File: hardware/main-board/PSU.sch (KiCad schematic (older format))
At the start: 5 parts, among them U3 AP1509-33SG-13

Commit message: added all 3d
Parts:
- L1: footprint Inductor_SMD:L_Taiyo-Yuden_NR-60xx -> main-board-custom-footprints:L_Taiyo-Yuden_NR-60xx
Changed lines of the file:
@@
 F 0 "L1" V 7040 5000 50  0000 C CNN
 F 1 "47uH" V 6949 5000 50  0000 C CNN
-F 2 "Inductor_SMD:L_Taiyo-Yuden_NR-60xx" H 6850 5000 50  0001 C CNN
+F 2 "main-board-custom-footprints:L_Taiyo-Yuden_NR-60xx" H 6850 5000 50  0001 C CNN
 F 3 "~" H 6850 5000 50  0001 C CNN
 F 4 "NRS6045T470MMGKV" V 6850 5000 50  0001 C CNN "MPN"

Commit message: SO-8 3d added, layout done
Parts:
- U3: footprint Package_SO:SO-8_3.9x4.9mm_P1.27mm -> main-board-custom-footprints:SO-8_3.9x4.9mm_P1.27mm
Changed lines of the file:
@@
 F 0 "U3" H 5800 5565 50  0000 C CNN
 F 1 "AP1509-33SG-13" H 5800 5474 50  0000 C CNN
-F 2 "Package_SO:SO-8_3.9x4.9mm_P1.27mm" H 5750 5250 50  0001 C CNN
+F 2 "main-board-custom-footprints:SO-8_3.9x4.9mm_P1.27mm" H 5750 5250 50  0001 C CNN
 F 3 "" H 5750 5250 50  0001 C CNN
 F 4 "AP1509-33SG-13" H 5800 5150 50  0001 C CNN "MPN"

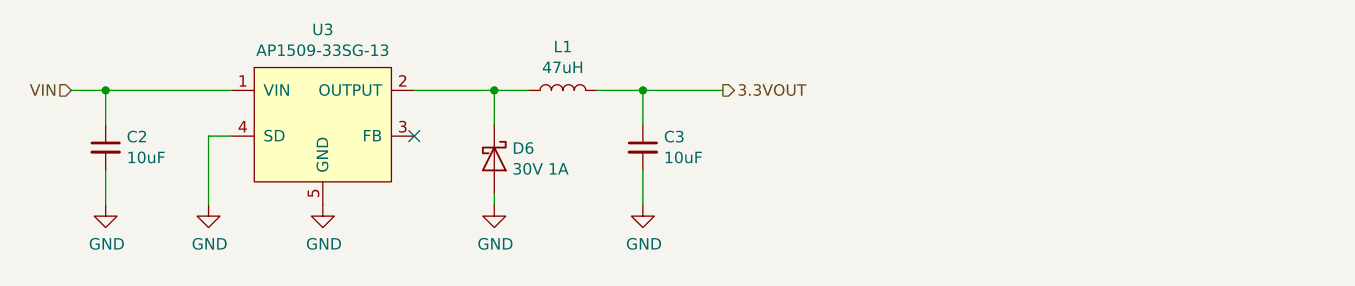
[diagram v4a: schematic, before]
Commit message: added qr code, switched button to a different button. put on reddit for review
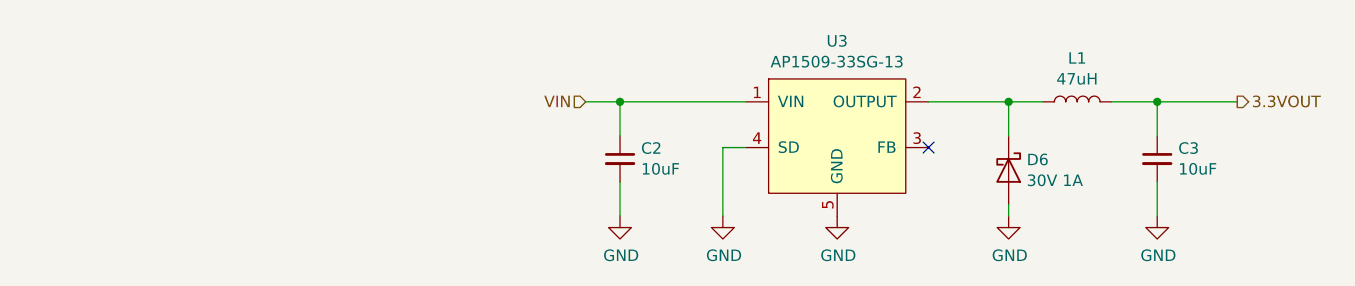
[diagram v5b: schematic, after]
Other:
- moved on the sheet: C2, C3, D6, L1, U3
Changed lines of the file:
@@
 EESchema Schematic File Version 4
-LIBS:main-board-cache
-EELAYER 29 0
+EELAYER 30 0
 EELAYER END
 $Descr B 17000 11000
@@
 L main-board-custom-symbols:AP1509-50 U3
 U 1 1 60FCBB15
-P 5800 5150
-F 0 "U3" H 5800 5565 50  0000 C CNN
-F 1 "AP1509-33SG-13" H 5800 5474 50  0000 C CNN
-F 2 "main-board-custom-footprints:SO-8_3.9x4.9mm_P1.27mm" H 5750 5250 50  0001 C CNN
-F 3 "" H 5750 5250 50  0001 C CNN
-F 4 "AP1509-33SG-13" H 5800 5150 50  0001 C CNN "MPN"
-	1    5800 5150
+P 8050 5200
+F 0 "U3" H 8050 5615 50  0000 C CNN
+F 1 "AP1509-33SG-13" H 8050 5524 50  0000 C CNN
+F 2 "main-board-custom-footprints:SO-8_3.9x4.9mm_P1.27mm" H 8000 5300 50  0001 C CNN
+F 3 "" H 8000 5300 50  0001 C CNN
+F 4 "AP1509-33SG-13" H 8050 5200 50  0001 C CNN "MPN"
+	1    8050 5200
 	1    0    0    -1
 $EndComp
-NoConn ~ 6200 5200
+NoConn ~ 8450 5250
 Wire Wire Line
-	5400 5200 5300 5200
+	7650 5250 7550 5250
 $Comp
 L power:GND #PWR019
 U 1 1 60FCC50A
-P 5800 5500
-F 0 "#PWR019" H 5800 5250 50  0001 C CNN
-F 1 "GND" H 5805 5327 50  0000 C CNN
-F 2 "" H 5800 5500 50  0001 C CNN
-F 3 "" H 5800 5500 50  0001 C CNN
-	1    5800 5500
+P 8050 5550
+F 0 "#PWR019" H 8050 5300 50  0001 C CNN
+F 1 "GND" H 8055 5377 50  0000 C CNN
+F 2 "" H 8050 5550 50  0001 C CNN
+F 3 "" H 8050 5550 50  0001 C CNN
+	1    8050 5550
 	1    0    0    -1
 $EndComp
@@
 L power:GND #PWR018
 U 1 1 60FCC70B
-P 5300 5500
-F 0 "#PWR018" H 5300 5250 50  0001 C CNN
-F 1 "GND" H 5305 5327 50  0000 C CNN
-F 2 "" H 5300 5500 50  0001 C CNN
-F 3 "" H 5300 5500 50  0001 C CNN
-	1    5300 5500
+P 7550 5550
+F 0 "#PWR018" H 7550 5300 50  0001 C CNN
+F 1 "GND" H 7555 5377 50  0000 C CNN
+F 2 "" H 7550 5550 50  0001 C CNN
+F 3 "" H 7550 5550 50  0001 C CNN
+	1    7550 5550
 	1    0    0    -1
 $EndComp
 Wire Wire Line
-	5300 5200 5300 5500
+	7550 5250 7550 5550
 $Comp
 L Device:C_Small C2
 U 1 1 60FCCE2C
-P 4850 5250
-F 0 "C2" H 4942 5296 50  0000 L CNN
-F 1 "10uF" H 4942 5205 50  0000 L CNN
-F 2 "Capacitor_SMD:C_1210_3225Metric" H 4850 5250 50  0001 C CNN
-F 3 "~" H 4850 5250 50  0001 C CNN
-	1    4850 5250
+P 7100 5300
+F 0 "C2" H 7192 5346 50  0000 L CNN
+F 1 "10uF" H 7192 5255 50  0000 L CNN
+F 2 "Capacitor_SMD:C_1210_3225Metric" H 7100 5300 50  0001 C CNN
+F 3 "~" H 7100 5300 50  0001 C CNN
+	1    7100 5300
 	1    0    0    -1
 $EndComp
 Wire Wire Line
-	5400 5000 4850 5000
+	7650 5050 7100 5050
 Wire Wire Line
-	4850 5000 4850 5150
+	7100 5050 7100 5200
 $Comp
 L power:GND #PWR017
 U 1 1 60FCD6A2
-P 4850 5500
-F 0 "#PWR017" H 4850 5250 50  0001 C CNN
-F 1 "GND" H 4855 5327 50  0000 C CNN
-F 2 "" H 4850 5500 50  0001 C CNN
-F 3 "" H 4850 5500 50  0001 C CNN
-	1    4850 5500
+P 7100 5550
+F 0 "#PWR017" H 7100 5300 50  0001 C CNN
+F 1 "GND" H 7105 5377 50  0000 C CNN
+F 2 "" H 7100 5550 50  0001 C CNN
+F 3 "" H 7100 5550 50  0001 C CNN
+	1    7100 5550
 	1    0    0    -1
 $EndComp
 Wire Wire Line
-	4850 5350 4850 5500
+	7100 5400 7100 5550
 $Comp
 L Device:D_Schottky D6
 U 1 1 60FCE5F1
-P 6550 5300
-F 0 "D6" V 6504 5379 50  0000 L CNN
-F 1 "30V 1A" V 6595 5379 50  0000 L CNN
-F 2 "Diode_SMD:D_SMA" H 6550 5300 50  0001 C CNN
-F 3 "~" H 6550 5300 50  0001 C CNN
-F 4 "SS13MHRSG" V 6550 5300 50  0001 C CNN "MPN"
-	1    6550 5300
+P 8800 5350
+F 0 "D6" V 8754 5429 50  0000 L CNN
+F 1 "30V 1A" V 8845 5429 50  0000 L CNN
+F 2 "Diode_SMD:D_SMA" H 8800 5350 50  0001 C CNN
+F 3 "~" H 8800 5350 50  0001 C CNN
+F 4 "SS13MHRSG" V 8800 5350 50  0001 C CNN "MPN"
+	1    8800 5350
 	0    1    1    0
 $EndComp
@@
 L power:GND #PWR020
 U 1 1 60FCEC10
-P 6550 5500
-F 0 "#PWR020" H 6550 5250 50  0001 C CNN
-F 1 "GND" H 6555 5327 50  0000 C CNN
-F 2 "" H 6550 5500 50  0001 C CNN
-F 3 "" H 6550 5500 50  0001 C CNN
-	1    6550 5500
+P 8800 5550
+F 0 "#PWR020" H 8800 5300 50  0001 C CNN
+F 1 "GND" H 8805 5377 50  0000 C CNN
+F 2 "" H 8800 5550 50  0001 C CNN
+F 3 "" H 8800 5550 50  0001 C CNN
+	1    8800 5550
 	1    0    0    -1
 $EndComp
 Wire Wire Line
-	6550 5450 6550 5500
+	8800 5500 8800 5550
 Wire Wire Line
-	6200 5000 6550 5000
+	8450 5050 8800 5050
 Wire Wire Line
-	6550 5000 6550 5150
+	8800 5050 8800 5200
 $Comp
 L Device:L L1
 U 1 1 60FCF9E1
-P 6850 5000
-F 0 "L1" V 7040 5000 50  0000 C CNN
-F 1 "47uH" V 6949 5000 50  0000 C CNN
-F 2 "main-board-custom-footprints:L_Taiyo-Yuden_NR-60xx" H 6850 5000 50  0001 C CNN
-F 3 "~" H 6850 5000 50  0001 C CNN
-F 4 "NRS6045T470MMGKV" V 6850 5000 50  0001 C CNN "MPN"
-	1    6850 5000
+P 9100 5050
+F 0 "L1" V 9290 5050 50  0000 C CNN
+F 1 "47uH" V 9199 5050 50  0000 C CNN
+F 2 "main-board-custom-footprints:L_Taiyo-Yuden_NR-60xx" H 9100 5050 50  0001 C CNN
+F 3 "~" H 9100 5050 50  0001 C CNN
+F 4 "NRS6045T470MMGKV" V 9100 5050 50  0001 C CNN "MPN"
+	1    9100 5050
 	0    -1   -1   0
 $EndComp
 Wire Wire Line
-	6550 5000 6700 5000
-Connection ~ 6550 5000
+	8800 5050 8950 5050
+Connection ~ 8800 5050
 $Comp
 L Device:C_Small C3
 U 1 1 60FCFF6B
-P 7200 5250
-F 0 "C3" H 7292 5296 50  0000 L CNN
-F 1 "10uF" H 7292 5205 50  0000 L CNN
-F 2 "Capacitor_SMD:C_0805_2012Metric" H 7200 5250 50  0001 C CNN
-F 3 "~" H 7200 5250 50  0001 C CNN
-	1    7200 5250
+P 9450 5300
+F 0 "C3" H 9542 5346 50  0000 L CNN
+F 1 "10uF" H 9542 5255 50  0000 L CNN
+F 2 "Capacitor_SMD:C_0805_2012Metric" H 9450 5300 50  0001 C CNN
+F 3 "~" H 9450 5300 50  0001 C CNN
+	1    9450 5300
 	1    0    0    -1
 $EndComp
 Wire Wire Line
-	7000 5000 7200 5000
+	9250 5050 9450 5050
 Wire Wire Line
-	7200 5000 7200 5150
+	9450 5050 9450 5200
 $Comp
 L power:GND #PWR021
 U 1 1 60FD0BAC
-P 7200 5500
-F 0 "#PWR021" H 7200 5250 50  0001 C CNN
-F 1 "GND" H 7205 5327 50  0000 C CNN
-F 2 "" H 7200 5500 50  0001 C CNN
-F 3 "" H 7200 5500 50  0001 C CNN
-	1    7200 5500
+P 9450 5550
+F 0 "#PWR021" H 9450 5300 50  0001 C CNN
+F 1 "GND" H 9455 5377 50  0000 C CNN
+F 2 "" H 9450 5550 50  0001 C CNN
+F 3 "" H 9450 5550 50  0001 C CNN
+	1    9450 5550
 	1    0    0    -1
 $EndComp
 Wire Wire Line
-	7200 5350 7200 5500
-Text HLabel 4700 5000 0    50   Input ~ 0
+	9450 5400 9450 5550
+Text HLabel 6950 5050 0    50   Input ~ 0
 VIN
 Wire Wire Line
-	7200 5000 7550 5000
-Connection ~ 7200 5000
-Text HLabel 7550 5000 2    50   Output ~ 0
+	9450 5050 9800 5050
+Connection ~ 9450 5050
+Text HLabel 9800 5050 2    50   Output ~ 0
 3.3VOUT
 Wire Wire Line
-	4700 5000 4850 5000
-Connection ~ 4850 5000
+	6950 5050 7100 5050
+Connection ~ 7100 5050
 $EndSCHEMATC

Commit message: BOM cleanup/adding MPNs
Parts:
- C2: MPN (none) -> C1210C106M3RACTU
- C3: MPN (none) -> CL21B106KQQNFNE
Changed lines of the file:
@@
 F 2 "Capacitor_SMD:C_1210_3225Metric" H 7100 5300 50  0001 C CNN
 F 3 "~" H 7100 5300 50  0001 C CNN
+F 4 "C1210C106M3RACTU" H 7100 5300 50  0001 C CNN "MPN"
 	1    7100 5300
 	1    0    0    -1
@@
 F 2 "Capacitor_SMD:C_0805_2012Metric" H 9450 5300 50  0001 C CNN
 F 3 "~" H 9450 5300 50  0001 C CNN
+F 4 "CL21B106KQQNFNE" H 9450 5300 50  0001 C CNN "MPN"
 	1    9450 5300
 	1    0    0    -1
